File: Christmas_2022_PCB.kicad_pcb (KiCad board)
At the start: 2 copper layers, 61.4 x 60.5 mm, 33 parts, among them J1 USB_A, J2 SOP8_test_point, J3 SOP8_test_point, SW1 SW_Push, SW2 SW_Push, SW3 SW_SPDT, U1 STM32F030K6Tx, U2 AMS1117-3.3

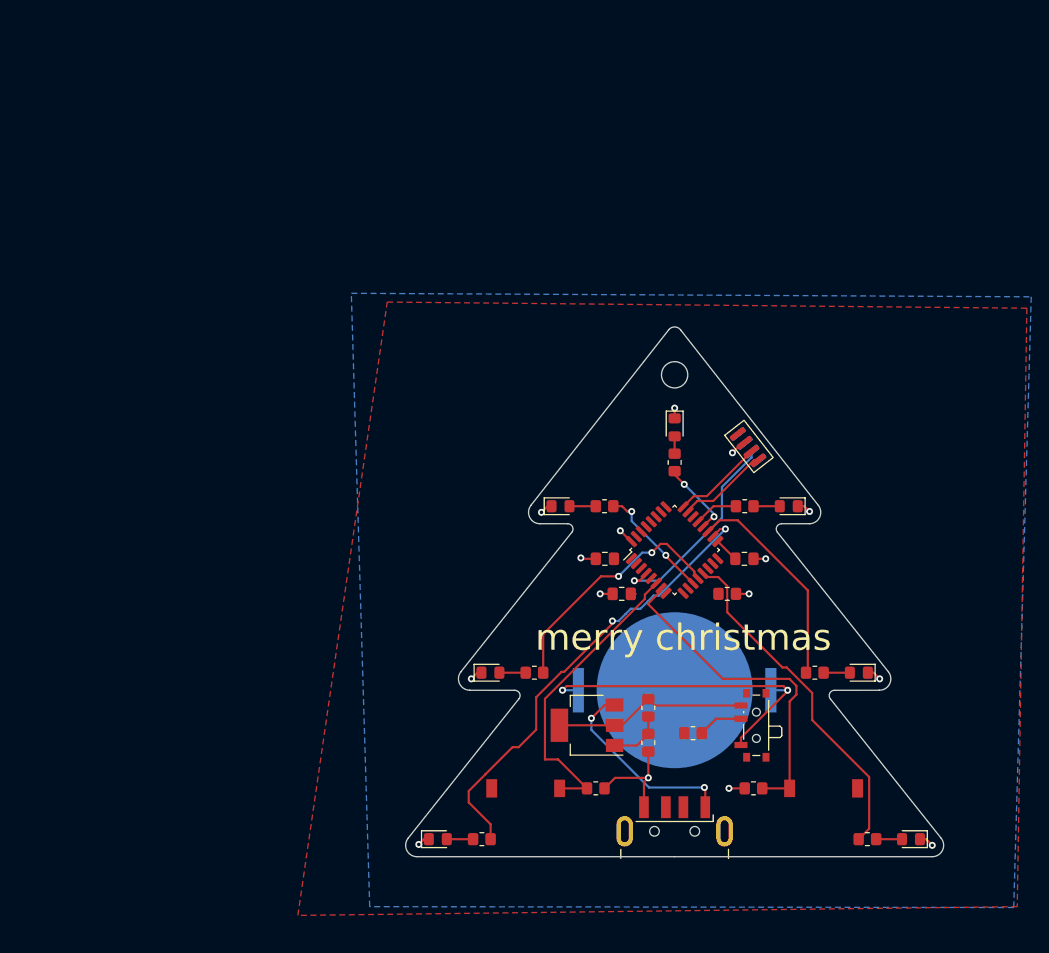
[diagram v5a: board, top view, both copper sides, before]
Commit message: Added secondary LEDs
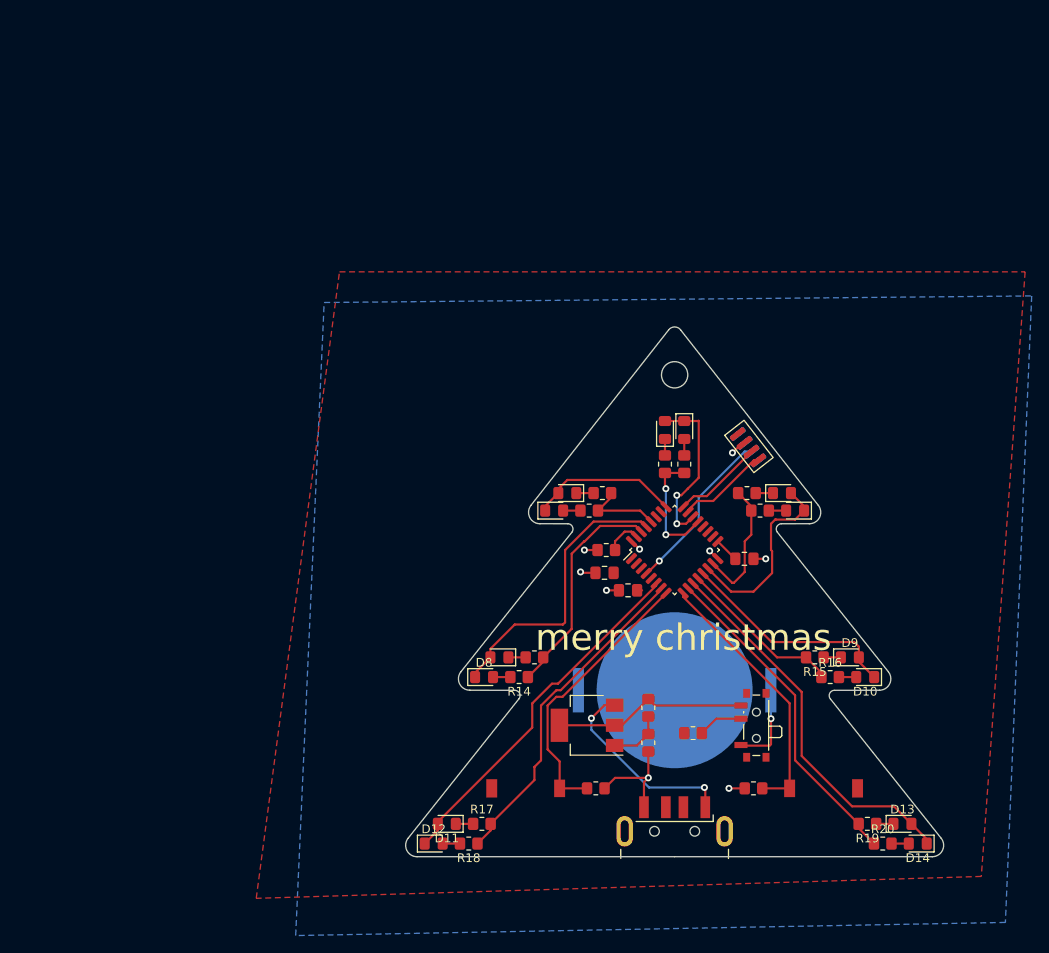
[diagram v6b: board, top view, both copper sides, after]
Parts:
- added D10: LED, LED_SMD:LED_0805_2012Metric_Pad1.15x1.40mm_HandSolder, F.Cu at (111.8, 89.5)
- added D11: LED, LED_SMD:LED_0805_2012Metric_Pad1.15x1.40mm_HandSolder, F.Cu at (64.0, 106.2)
- added D12: LED, LED_SMD:LED_0805_2012Metric_Pad1.15x1.40mm_HandSolder, F.Cu at (62.5, 108.5)
- added D13: LED, LED_SMD:LED_0805_2012Metric_Pad1.15x1.40mm_HandSolder, F.Cu at (116.0, 106.2)
- added D14: LED, LED_SMD:LED_0805_2012Metric_Pad1.15x1.40mm_HandSolder, F.Cu at (117.8, 108.5)
- added D8: LED, LED_SMD:LED_0805_2012Metric_Pad1.15x1.40mm_HandSolder, F.Cu at (68.2, 89.5)
- added D9: LED, LED_SMD:LED_0805_2012Metric_Pad1.15x1.40mm_HandSolder, F.Cu at (110.0, 87.2)
- added R14: R, Resistor_SMD:R_0805_2012Metric_Pad1.20x1.40mm_HandSolder, F.Cu at (72.2, 89.5)
- added R15: R, Resistor_SMD:R_0805_2012Metric_Pad1.20x1.40mm_HandSolder, F.Cu at (106.0, 87.2)
- added R16: R, Resistor_SMD:R_0805_2012Metric_Pad1.20x1.40mm_HandSolder, F.Cu at (107.8, 89.5)
- added R17: R, Resistor_SMD:R_0805_2012Metric_Pad1.20x1.40mm_HandSolder, F.Cu at (68.0, 106.2)
- added R18: R, Resistor_SMD:R_0805_2012Metric_Pad1.20x1.40mm_HandSolder, F.Cu at (66.5, 108.5)
- added R19: R, Resistor_SMD:R_0805_2012Metric_Pad1.20x1.40mm_HandSolder, F.Cu at (112.0, 106.2)
- added R20: R, Resistor_SMD:R_0805_2012Metric_Pad1.20x1.40mm_HandSolder, F.Cu at (113.8, 108.5)
- moved D3 55.7 mm to (77.8, 68.5)
- moved R7 47.6 mm to (91.1, 65.2), turned to 90 degrees
- moved R9 41.8 mm to (81.8, 68.5), turned to 0 degrees
- moved D4 39.8 mm to (76.2, 70.5)
- moved D7 37.3 mm to (70.0, 87.2)
- moved D2 35.5 mm to (91.1, 61.3), turned to -90 degrees
- moved R13 29.6 mm to (74.0, 87.2)
- moved D5 22.3 mm to (102.2, 68.5), turned to 0 degrees
- moved R10 21.9 mm to (98.2, 68.5), turned to 180 degrees
- moved R6 19.5 mm to (80.2, 70.5)
- moved D6 16.7 mm to (103.8, 70.5), turned to 180 degrees
- moved D1 14.8 mm to (88.9, 61.3), turned to 90 degrees
- moved R1 14.7 mm to (82.2, 75.0), turned to 180 degrees
- moved R12 11.2 mm to (99.8, 70.5), turned to 0 degrees
- moved R5 8.41 mm to (88.9, 65.2), turned to -90 degrees
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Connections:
- D1 pad 1: GND -> Net-(D1-Pad1)
- D1 pad 2: Net-(D1-Pad2) -> /IO_GEN
- D2 pad 1: GND -> /IO_GEN
- D3 pad 1: GND -> Net-(D3-Pad1)
- D3 pad 2: Net-(D3-Pad2) -> /IO_GEN
- D4 pad 1: GND -> /IO_GEN
- D5 pad 1: GND -> Net-(D5-Pad1)
- D5 pad 2: Net-(D5-Pad2) -> /IO_GEN
- D6 pad 1: GND -> /IO_GEN
- D7 pad 1: GND -> Net-(D7-Pad1)
- D7 pad 2: Net-(D7-Pad2) -> /IO_GEN
- R10 pad 1: /LED5 -> Net-(D5-Pad1)
- R10 pad 2: Net-(D5-Pad2) -> /IO_GEN
- R12 pad 1: /LED6 -> /IO_GEN
- R13 pad 1: /LED7 -> Net-(D7-Pad1)
- R13 pad 2: Net-(D7-Pad2) -> /IO_GEN
- R4 pad 2: /BUT_LEFT -> /IO_GEN
- R5 pad 1: /LED1 -> Net-(D1-Pad1)
- R5 pad 2: Net-(D1-Pad2) -> /IO_GEN
- R6 pad 1: /LED2 -> /IO_GEN
- R6 pad 2: Net-(D2-Pad2) -> Net-(D4-Pad2)
- R7 pad 1: /LED3 -> /IO_GEN
- R7 pad 2: Net-(D3-Pad2) -> Net-(D2-Pad2)
- R8 pad 2: /BUT_RIGHT -> /IO_GEN
- R9 pad 1: /LED4 -> Net-(D3-Pad1)
- R9 pad 2: Net-(D4-Pad2) -> /IO_GEN
- SW1 pad 2: /BUT_LEFT -> /IO_GEN
- SW2 pad 2: /BUT_RIGHT -> /IO_GEN
- U1 pad 10: unconnected-(U1-Pad10) -> /IO_GEN
- U1 pad 11: /LED1 -> /IO_GEN
- U1 pad 12: /LED2 -> /IO_GEN
- U1 pad 13: /LED3 -> /IO_GEN
- U1 pad 14: unconnected-(U1-Pad14) -> /IO_GEN
- U1 pad 15: unconnected-(U1-Pad15) -> /IO_GEN
- U1 pad 18: /LED4 -> /IO_GEN
- U1 pad 19: /LED5 -> /IO_GEN
- U1 pad 20: /LED6 -> /IO_GEN
- U1 pad 21: /LED7 -> /IO_GEN
- U1 pad 22: unconnected-(U1-Pad22) -> /IO_GEN
- U1 pad 25: unconnected-(U1-Pad25) -> /IO_GEN
- U1 pad 28: unconnected-(U1-Pad28) -> /IO_GEN
- U1 pad 29: unconnected-(U1-Pad29) -> /IO_GEN
- U1 pad 30: unconnected-(U1-Pad30) -> /IO_GEN
- U1 pad 6: /BUT_LEFT -> /IO_GEN
- U1 pad 7: /BUT_RIGHT -> /IO_GEN
- U1 pad 8: unconnected-(U1-Pad8) -> /IO_GEN
- U1 pad 9: unconnected-(U1-Pad9) -> /IO_GEN
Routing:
- net /IO_GEN: track 0.00 -> 422.1 mm, vias 0 -> 4
- net /LED4: track 52.4 -> 0.00 mm, vias 2 -> 0
- net /LED3: track 39.8 -> 0.00 mm
- net /BUT_RIGHT: track 38.3 -> 0.00 mm
- net /BUT_LEFT: track 34.7 -> 0.00 mm
- net /VBATT: track 38.3 -> 9.70 mm, vias 2 -> 1
- net /LED2: track 28.2 -> 0.00 mm, vias 2 -> 0
- net /LED5: track 24.7 -> 0.00 mm
- net /LED1: track 13.5 -> 0.00 mm, vias 2 -> 0
- net GND: track 33.9 -> 24.4 mm, vias 15 -> 9
- net /LED6: track 8.80 -> 0.00 mm, vias 2 -> 0
- net /LED7: track 5.06 -> 0.00 mm
- net /NRST: track 23.7 -> 19.4 mm
- net Net-(R1-Pad1): track 0.59 -> 4.12 mm
- net Net-(D7-Pad2): track 3.00 -> 0.00 mm
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
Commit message: finished routing. Added missing 3D models
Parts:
- removed R2, R3: R, Resistor_SMD:R_0805_2012Metric_Pad1.20x1.40mm_HandSolder
- moved SW3 2.97 mm to (96.0, 95.0)
- moved R11 2.74 mm to (89.8, 94.5), turned to -90 degrees
- moved U2 1.75 mm to (81.8, 95.0)
- moved R5 1.30 mm to (88.9, 63.9)
- moved R7 1.30 mm to (91.1, 63.9)
- moved D1 1.30 mm to (88.9, 60.0)
- moved D2 1.30 mm to (91.1, 60.0)
- moved BT1 1.27 mm to (89.8, 92.2), turned to 0 degrees
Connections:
- D1 pad 2: /IO_GEN -> /LED2
- D10 pad 1: /IO_GEN -> /LED10
- D11 pad 2: /IO_GEN -> /LED12
- D12 pad 1: /IO_GEN -> /LED12
- D13 pad 2: /IO_GEN -> /LED14
- D14 pad 1: /IO_GEN -> /LED14
- D2 pad 1: /IO_GEN -> /LED2
- D3 pad 2: /IO_GEN -> /LED4
- D4 pad 1: /IO_GEN -> /LED4
- D5 pad 2: /IO_GEN -> /LED6
- D6 pad 1: /IO_GEN -> /LED6
- D7 pad 2: /IO_GEN -> /LED8
- D8 pad 1: /IO_GEN -> /LED8
- D9 pad 2: /IO_GEN -> /LED10
- R10 pad 2: /IO_GEN -> /LED5
- R12 pad 1: /IO_GEN -> /LED5
- R13 pad 2: /IO_GEN -> /LED7
- R14 pad 1: /IO_GEN -> /LED7
- R15 pad 2: /IO_GEN -> /LED9
- R16 pad 1: /IO_GEN -> /LED9
- R17 pad 2: /IO_GEN -> /LED11
- R18 pad 1: /IO_GEN -> /LED11
- R19 pad 2: /IO_GEN -> /LED13
- R20 pad 1: /IO_GEN -> /LED13
- R4 pad 2: /IO_GEN -> /SW_LEFT
- R5 pad 2: /IO_GEN -> /LED1
- R6 pad 1: /IO_GEN -> /LED3
- R7 pad 1: /IO_GEN -> /LED1
- R8 pad 2: /IO_GEN -> /SW_RIGHT
- R9 pad 2: /IO_GEN -> /LED3
- SW1 pad 2: /IO_GEN -> /SW_LEFT
- SW2 pad 2: /IO_GEN -> /SW_RIGHT
- U1 pad 10: /IO_GEN -> /LED13
- U1 pad 11: /IO_GEN -> /LED14
- U1 pad 12: /IO_GEN -> /LED9
- U1 pad 13: /IO_GEN -> /LED10
- U1 pad 14: /IO_GEN -> /LED6
- U1 pad 15: /IO_GEN -> /LED5
- U1 pad 18: /IO_GEN -> unconnected-(U1-Pad18)
- U1 pad 19: /IO_GEN -> unconnected-(U1-Pad19)
- U1 pad 20: /IO_GEN -> unconnected-(U1-Pad20)
- U1 pad 21: /IO_GEN -> /LED1
- U1 pad 22: /IO_GEN -> /LED2
- U1 pad 25: /IO_GEN -> /LED4
- U1 pad 28: /IO_GEN -> /LED3
- U1 pad 29: /IO_GEN -> /LED8
- U1 pad 30: /IO_GEN -> /LED7
- U1 pad 6: /IO_GEN -> /LED12
- U1 pad 7: /IO_GEN -> /LED11
- U1 pad 8: /IO_GEN -> /SW_LEFT
- U1 pad 9: /IO_GEN -> /SW_RIGHT
- U2 pad 1: Net-(R2-Pad2) -> GND
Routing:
- net /IO_GEN: track 422.1 -> 0.00 mm, vias 4 -> 0
- net +3V3: track 3.38 -> 63.3 mm, vias 0 -> 11
- net /LED14: track 0.00 -> 43.5 mm
- net /LED12: track 0.00 -> 41.8 mm
- net /LED11: track 0.00 -> 39.1 mm
- net /LED13: track 0.00 -> 37.9 mm
- net /VBATT: track 9.70 -> 42.6 mm, vias 1 -> 2
- net /LED8: track 0.00 -> 32.8 mm
- net /SW_LEFT: track 0.00 -> 32.6 mm
- net /SW_RIGHT: track 0.00 -> 30.4 mm
- net /LED7: track 0.00 -> 25.7 mm
- net /LED10: track 0.00 -> 25.5 mm
- net /LED6: track 0.00 -> 22.0 mm
- net /LED9: track 0.00 -> 19.0 mm
- net /LED2: track 0.00 -> 18.6 mm, vias 0 -> 2
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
